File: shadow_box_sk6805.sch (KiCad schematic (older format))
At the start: 20 parts, among them J1 USB_B_Micro, U1 ATtiny88-AU, U2 MCP7940N-xST, Y1 7pF CL

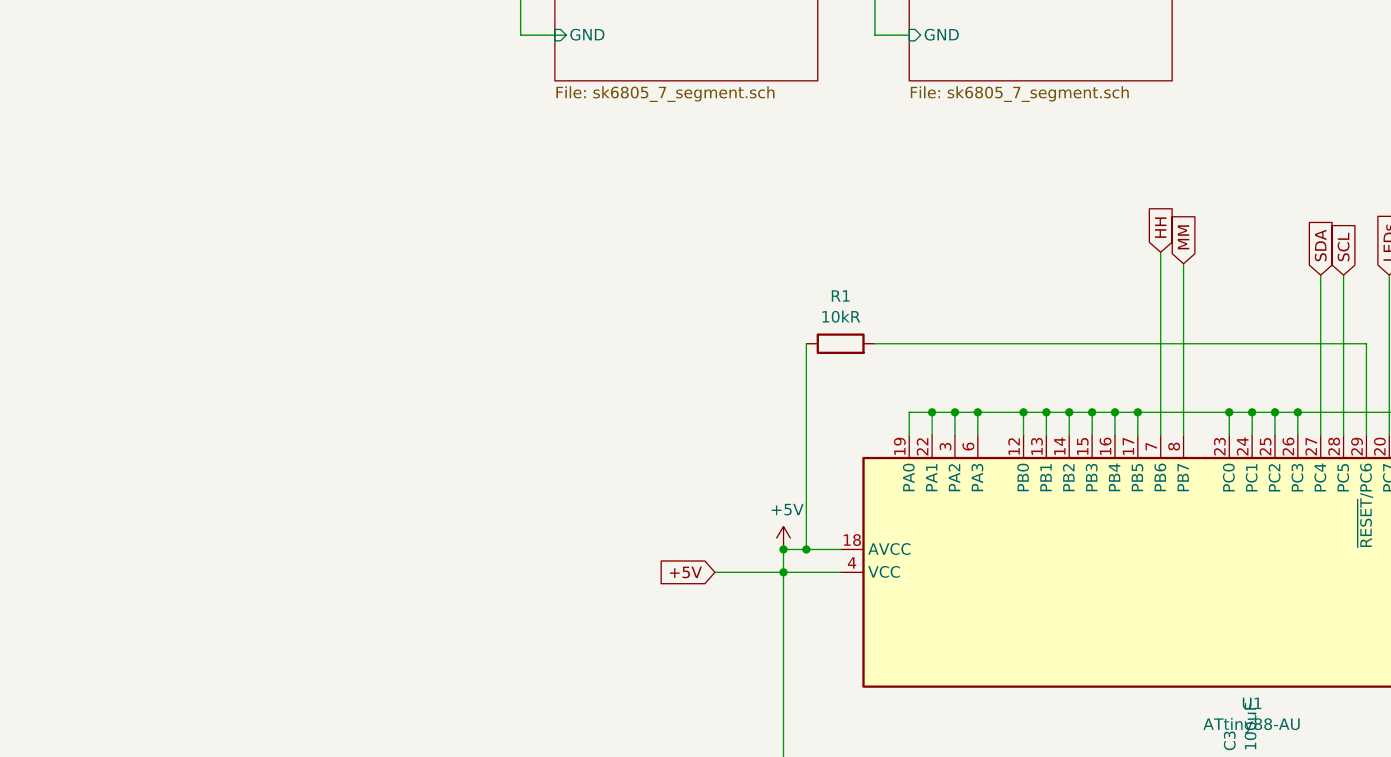
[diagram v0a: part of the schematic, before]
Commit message: Add ISP header, wire up everything
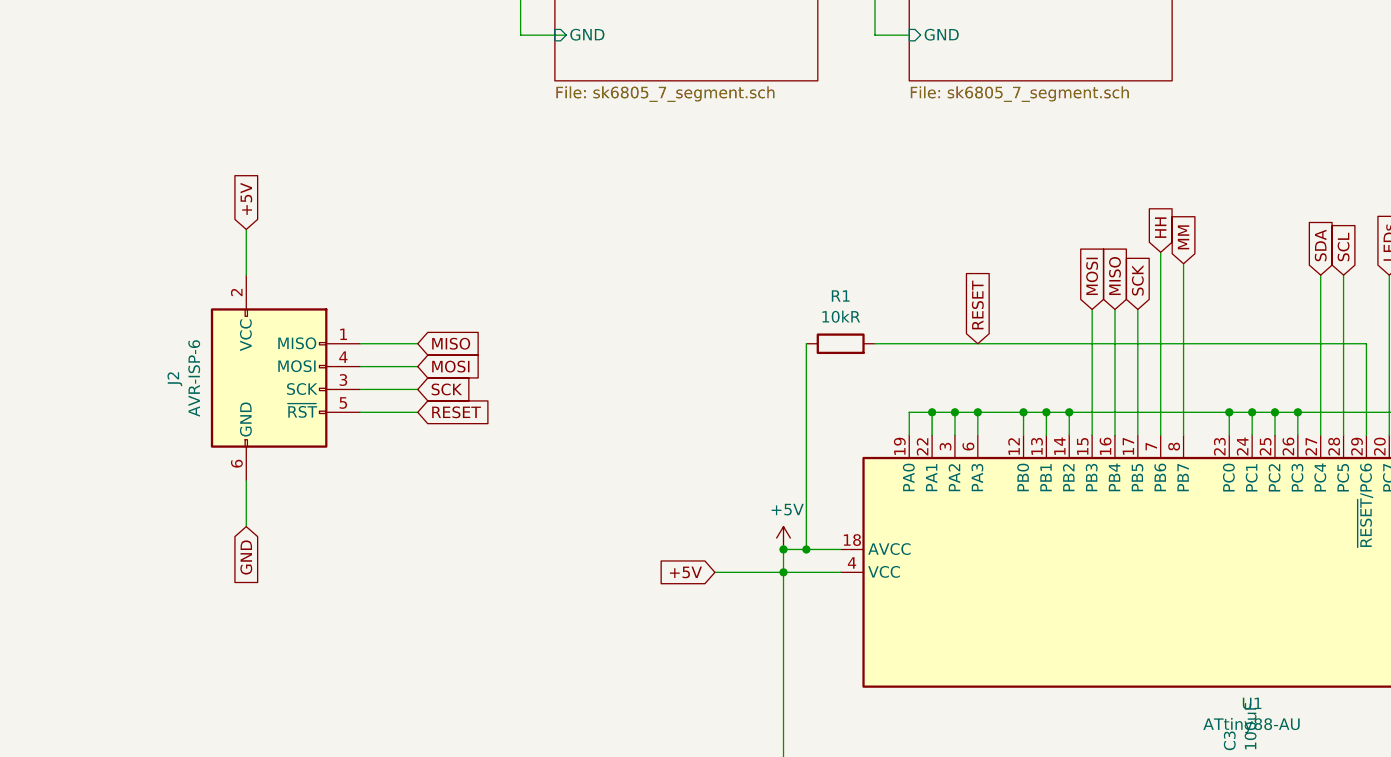
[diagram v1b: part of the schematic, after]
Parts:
- added J2: AVR-ISP-6, Connector_PinHeader_2.54mm:PinHeader_2x03_P2.54mm_Vertical_SMD, symbol Connector:AVR-ISP-6
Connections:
- net +5V: now also J2.2 (VCC)
- net GND: now also J2.6 (GND); no longer U1.15 (PB3), U1.16 (PB4), U1.17 (PB5)
- net RESET: now reaches R1.2, U1.29 (~RESET~/PC6)
- net RESET: now also J2.5 (~RST)
- new net MISO: J2.1 (MISO), U1.16 (PB4)
- new net MOSI: J2.4 (MOSI), U1.15 (PB3)
- new net SCK: J2.3 (SCK), U1.17 (PB5)
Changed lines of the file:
@@
 MM
-Wire Wire Line
-	7100 4250 9250 4250
 Wire Wire Line
 	8350 3850 8350 4650
@@
 Connection ~ 7950 4550
 Wire Wire Line
-	7950 4550 8050 4550
-Wire Wire Line
-	8050 4650 8050 4550
-Connection ~ 8050 4550
-Wire Wire Line
-	8050 4550 8150 4550
-Wire Wire Line
-	8150 4650 8150 4550
-Connection ~ 8150 4550
-Wire Wire Line
-	8150 4550 8250 4550
-Wire Wire Line
-	8250 4650 8250 4550
-Connection ~ 8250 4550
-Wire Wire Line
-	8250 4550 8650 4550
-Wire Wire Line
 	8650 4650 8650 4550
 Connection ~ 8650 4550
@@
 Wire Wire Line
 	5350 1900 5350 2700
+$Comp
+L Connector:AVR-ISP-6 J2
+U 1 1 5E96D5D8
+P 4450 4450
+F 0 "J2" V 4033 4500 50  0000 C CNN
+F 1 "AVR-ISP-6" V 4124 4500 50  0000 C CNN
+F 2 "Connector_PinHeader_2.54mm:PinHeader_2x03_P2.54mm_Vertical_SMD" V 4200 4500 50  0001 C CNN
+F 3 " ~" H 3175 3900 50  0001 C CNN
+	1    4450 4450
+	1    0    0    -1
+$EndComp
+Wire Wire Line
+	7100 4250 9250 4250
+Text GLabel 5100 4550 2    50   Input ~ 0
+RESET
+Text GLabel 5100 4450 2    50   Input ~ 0
+SCK
+Text GLabel 5100 4350 2    50   Input ~ 0
+MOSI
+Text GLabel 5100 4250 2    50   Input ~ 0
+MISO
+Text GLabel 4350 3750 1    50   Input ~ 0
++5V
+Text GLabel 4350 5050 3    50   Input ~ 0
+GND
+Wire Wire Line
+	4350 3750 4350 3950
+Wire Wire Line
+	4350 4850 4350 5050
+Wire Wire Line
+	4850 4550 5100 4550
+Wire Wire Line
+	5100 4450 4850 4450
+Wire Wire Line
+	4850 4350 5100 4350
+Wire Wire Line
+	5100 4250 4850 4250
+Text GLabel 7550 4250 1    50   Input ~ 0
+RESET
+Wire Wire Line
+	7950 4550 8650 4550
+Text GLabel 8250 4100 1    50   Input ~ 0
+SCK
+Text GLabel 8050 4100 1    50   Input ~ 0
+MOSI
+Text GLabel 8150 4100 1    50   Input ~ 0
+MISO
+Wire Wire Line
+	8050 4100 8050 4650
+Wire Wire Line
+	8150 4650 8150 4100
+Wire Wire Line
+	8250 4100 8250 4650
 $EndSCHEMATC

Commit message: Update usb position, byline
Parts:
- J2: symbol Connector:AVR-ISP-6 -> shadow_box_sk6805-rescue:AVR-ISP-6-Connector
- U1: symbol MCU_Microchip_ATtiny:ATtiny88-AU -> shadow_box_sk6805-rescue:ATtiny88-AU-MCU_Microchip_ATtiny
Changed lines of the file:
@@
 EESchema Schematic File Version 4
-LIBS:shadow_box_sk6805-cache
-EELAYER 29 0
+EELAYER 30 0
 EELAYER END
 $Descr A4 11693 8268
@@
 	2500 1550 2650 1550
 $Comp
-L MCU_Microchip_ATtiny:ATtiny88-AU U1
+L shadow_box_sk6805-rescue:ATtiny88-AU-MCU_Microchip_ATtiny U1
 U 1 1 5E93A77C
 P 8750 5250
@@
 	5350 1900 5350 2700
 $Comp
-L Connector:AVR-ISP-6 J2
+L shadow_box_sk6805-rescue:AVR-ISP-6-Connector J2
 U 1 1 5E96D5D8
 P 4450 4450
